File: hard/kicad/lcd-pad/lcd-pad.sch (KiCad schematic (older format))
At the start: 5 parts, among them J1 VIAport

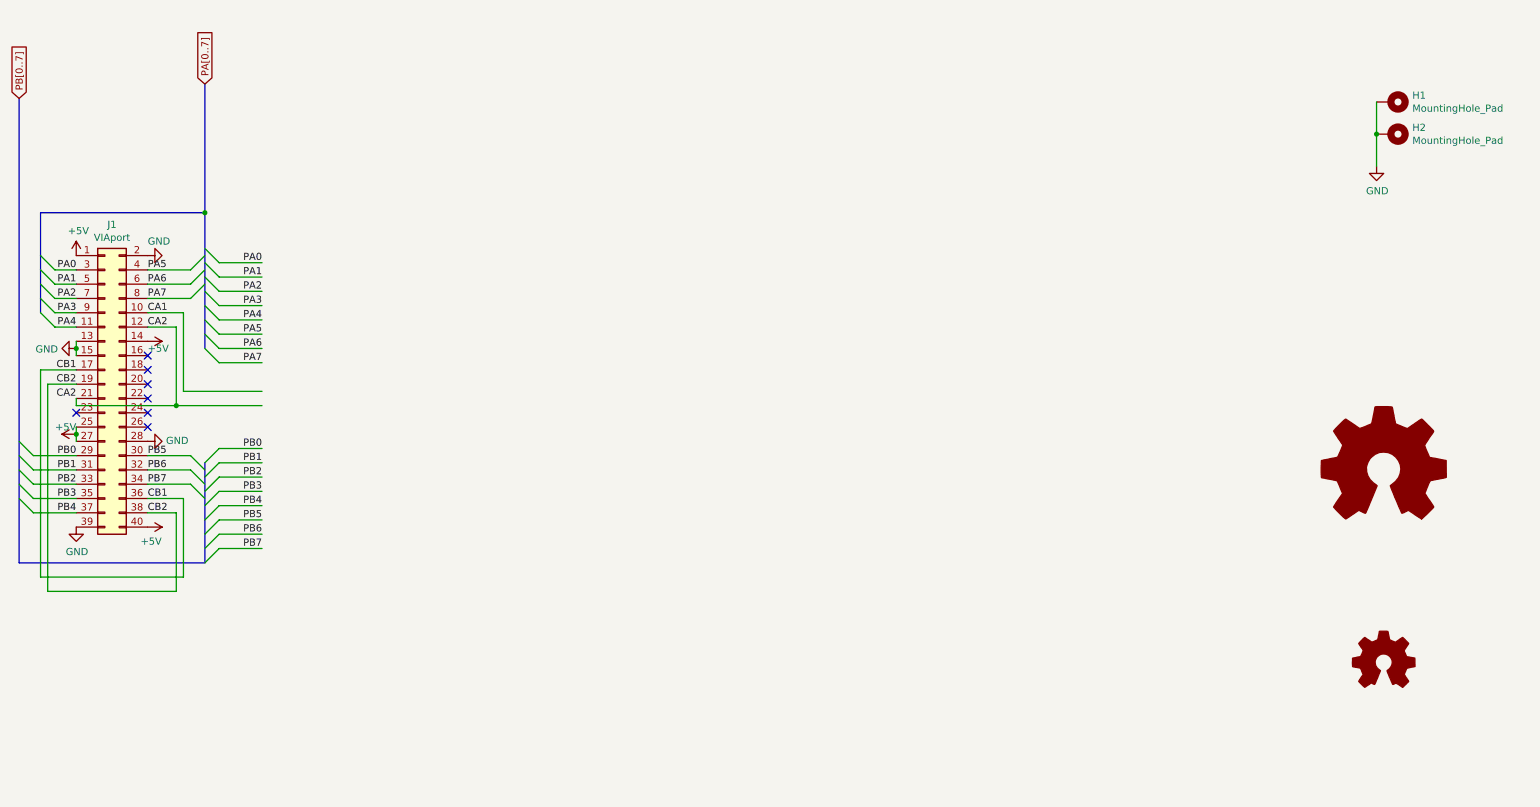
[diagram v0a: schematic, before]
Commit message: fix EIA v2.2
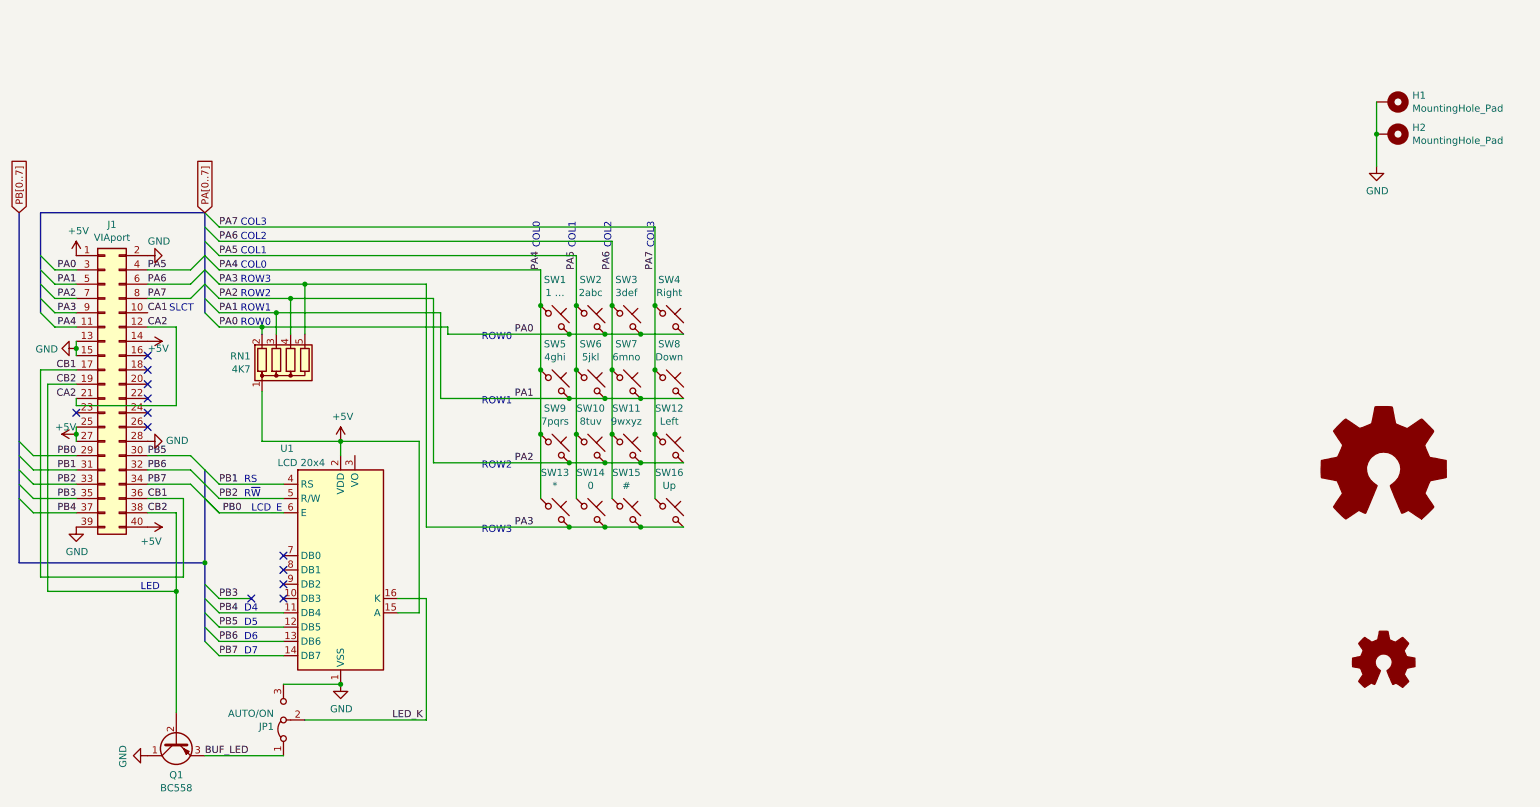
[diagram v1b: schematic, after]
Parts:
- added JP1: AUTO/ON, Connector_PinHeader_2.54mm:PinHeader_1x03_P2.54mm_Horizontal, symbol Jumper:Jumper_3_Bridged12
- added Q1: BC558, Package_TO_SOT_THT:TO-92_Inline, symbol Transistor_BJT:BC558
- added RN1: 4K7, Resistor_THT:R_Array_SIP5, symbol Device:R_Network04
- added SW1: 1 …, Button_Switch_THT:SW_PUSH_6mm, symbol Switch:SW_Push_45deg
- added SW10: 8tuv, Button_Switch_THT:SW_PUSH_6mm, symbol Switch:SW_Push_45deg
- added SW11: 9wxyz, Button_Switch_THT:SW_PUSH_6mm, symbol Switch:SW_Push_45deg
- added SW12: Left, Button_Switch_THT:SW_PUSH_6mm, symbol Switch:SW_Push_45deg
- added SW13: *, Button_Switch_THT:SW_PUSH_6mm, symbol Switch:SW_Push_45deg
- added SW14: 0, Button_Switch_THT:SW_PUSH_6mm, symbol Switch:SW_Push_45deg
- added SW15: #, Button_Switch_THT:SW_PUSH_6mm, symbol Switch:SW_Push_45deg
- added SW16: Up, Button_Switch_THT:SW_PUSH_6mm, symbol Switch:SW_Push_45deg
- added SW2: 2abc, Button_Switch_THT:SW_PUSH_6mm, symbol Switch:SW_Push_45deg
- added SW3: 3def, Button_Switch_THT:SW_PUSH_6mm, symbol Switch:SW_Push_45deg
- added SW4: Right, Button_Switch_THT:SW_PUSH_6mm, symbol Switch:SW_Push_45deg
- added SW5: 4ghi, Button_Switch_THT:SW_PUSH_6mm, symbol Switch:SW_Push_45deg
- added SW6: 5jkl, Button_Switch_THT:SW_PUSH_6mm, symbol Switch:SW_Push_45deg
- added SW7: 6mno, Button_Switch_THT:SW_PUSH_6mm, symbol Switch:SW_Push_45deg
- added SW8: Down, Button_Switch_THT:SW_PUSH_6mm, symbol Switch:SW_Push_45deg
- added SW9: 7pqrs, Button_Switch_THT:SW_PUSH_6mm, symbol Switch:SW_Push_45deg
- added U1: LCD 20x4, Display:JHD204AO_LCD20x4, symbol Display_Character:NHD-0420H1Z
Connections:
- net labels added: BUF_LED, LED_K
- wire segments 56 -> 108
- no-connect marks 7 -> 12
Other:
- note added: "COL0"
- note added: "COL1"
- note added: "COL2"
- note added: "COL3"
- note added: "D4"
- note added: "D5"
- note added: "D6"
- note added: "D7"
- note added: "LCD_E"
- note added: "LED"
- note added: "ROW0"
- note added: "ROW1"
- note added: "ROW2"
- note added: "ROW3"
- note added: "RS"
- note added: "R~W"
- note added: "SLCT"
